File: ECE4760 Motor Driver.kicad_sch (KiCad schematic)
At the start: 45 parts, among them J1 IO, J100 Alternative Motor, J2 Motor / Power, J4 UART, J5 Debug, SW1 BOOT, U1 STM32G473V_B-C-E_Hx, U5 AP7361C-33FGE, U7 TPSM365R6, X1 48MHz

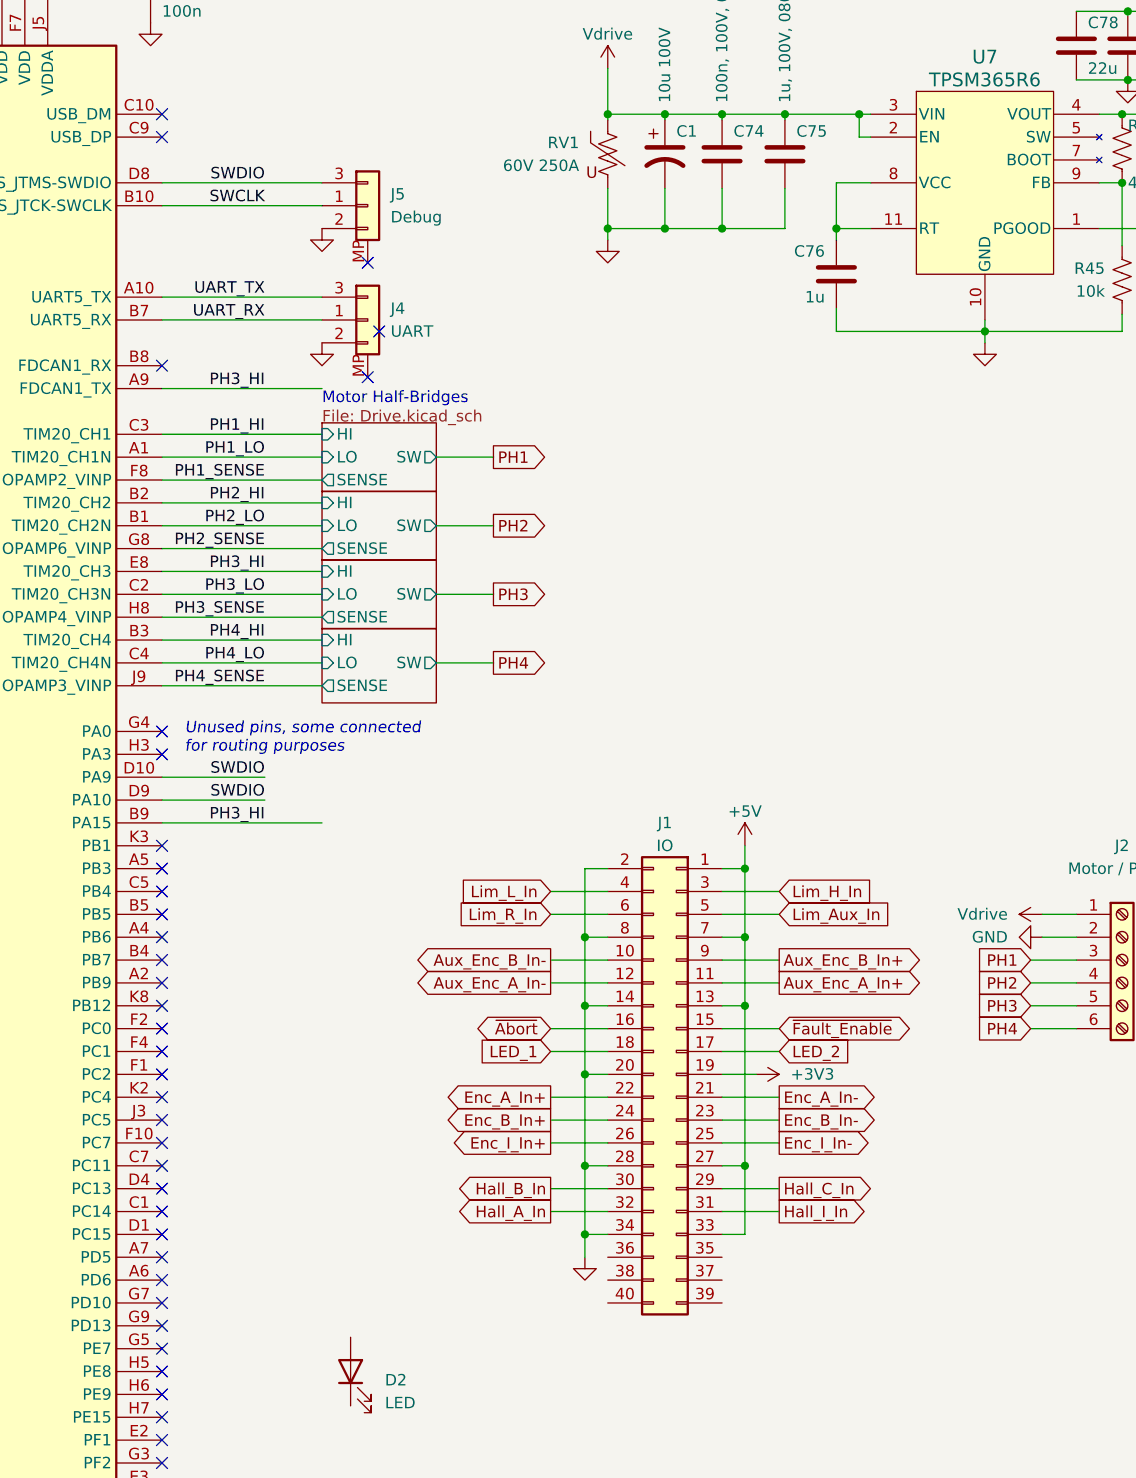
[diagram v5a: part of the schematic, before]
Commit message: Limit switch inputs and silkscreen
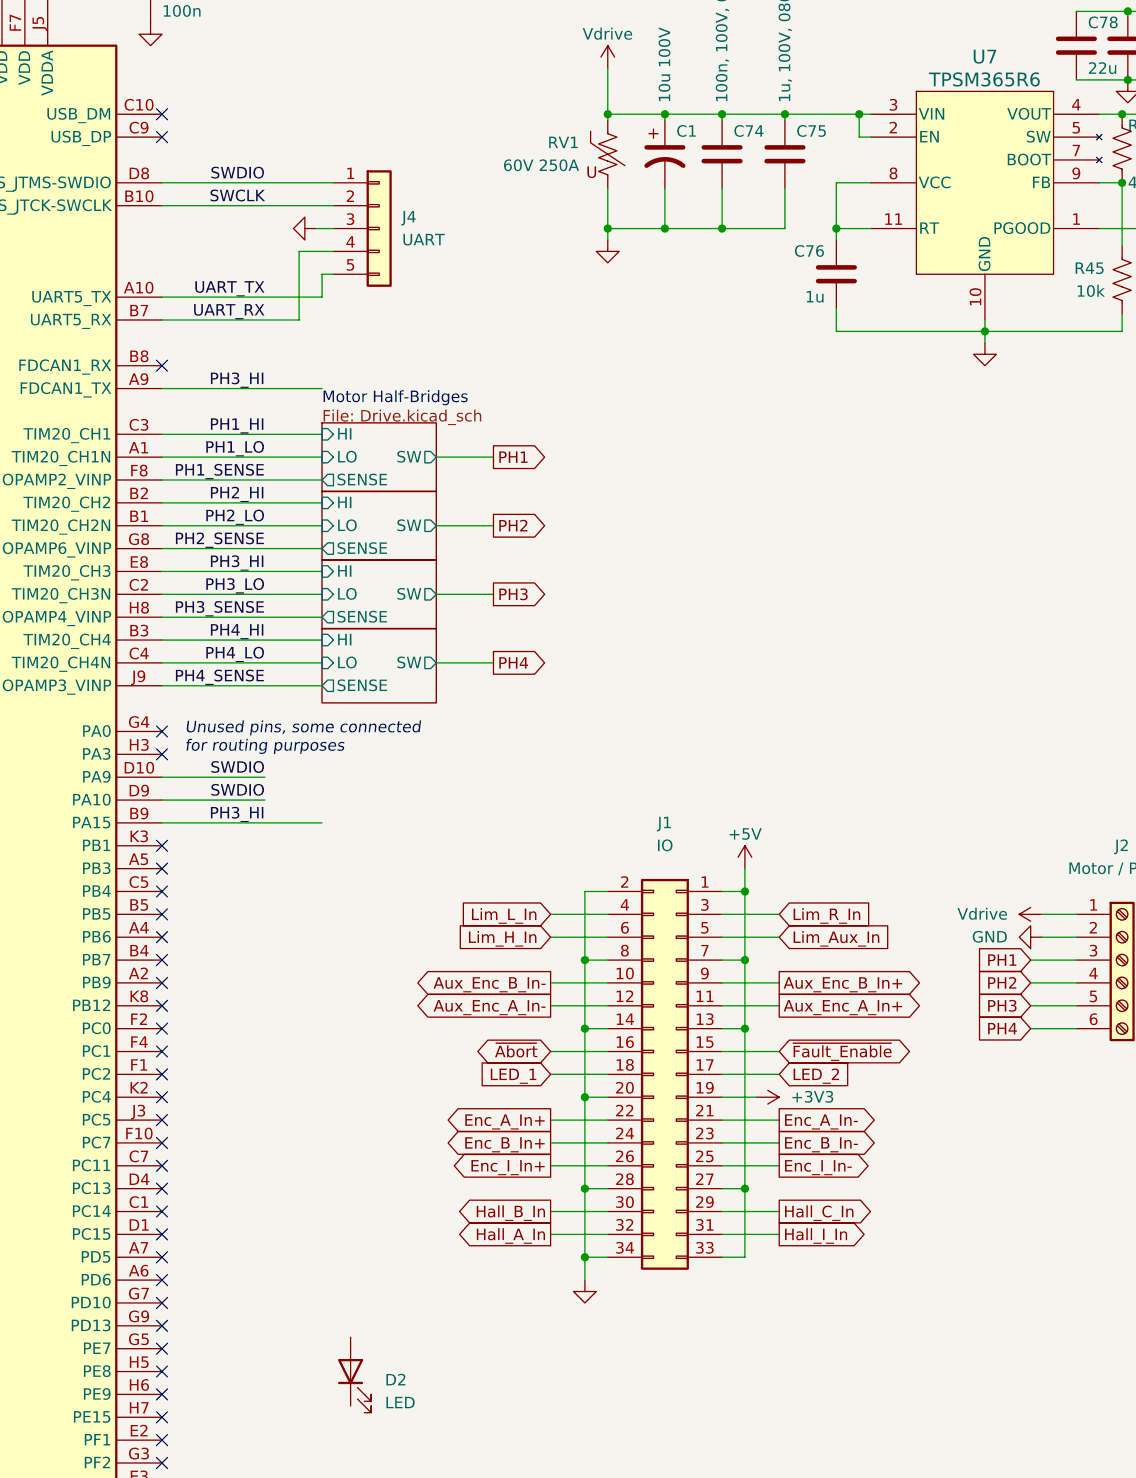
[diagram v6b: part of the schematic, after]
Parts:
- removed J5: Debug, Connector_JST:JST_GH_SM03B-GHS-TB_1x03-1MP_P1.25mm_Horizontal, symbol Connector_Generic:Conn_01x03
- C1: footprint Capacitor_THT:CP_Radial_D8.0mm_P5.00mm -> Capacitor_SMD:CP_Elec_6.3x7.7; DigiKey 1189-1513-1-ND -> (none); LCSC (none) -> C7471882
- J1: footprint Connector_PinSocket_2.54mm:PinSocket_2x20_P2.54mm_Vertical -> Connector_PinSocket_2.54mm:PinSocket_2x17_P2.54mm_Vertical; symbol Connector_Generic:Conn_02x20_Odd_Even -> Connector_Generic:Conn_02x17_Odd_Even
- J4: footprint Connector_JST:JST_GH_SM03B-GHS-TB_1x03-1MP_P1.25mm_Horizontal -> Connector_PinHeader_2.54mm:PinHeader_1x05_P2.54mm_Vertical; symbol Connector_Generic:Conn_01x03 -> Connector_Generic:Conn_01x05; DigiKey 455-SM03B-GHS-TBCT-ND -> (none); LCSC C514175 -> (none)
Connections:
- net GND: now also J4.3 (Pin_3); no longer J4.2 (Pin_2)
- net Lim_H_In: now also J1.6 (Pin_6); no longer J1.3 (Pin_3)
- net Lim_R_In: now also J1.3 (Pin_3); no longer J1.6 (Pin_6)
- net SWCLK: now also J4.2 (Pin_2)
- net SWDIO: now also J4.1 (Pin_1)
- net UART_RX: now also J4.4 (Pin_4); no longer J4.1 (Pin_1)
- net UART_TX: now also J4.5 (Pin_5); no longer J4.3 (Pin_3)
- no-connect marks 43 -> 40

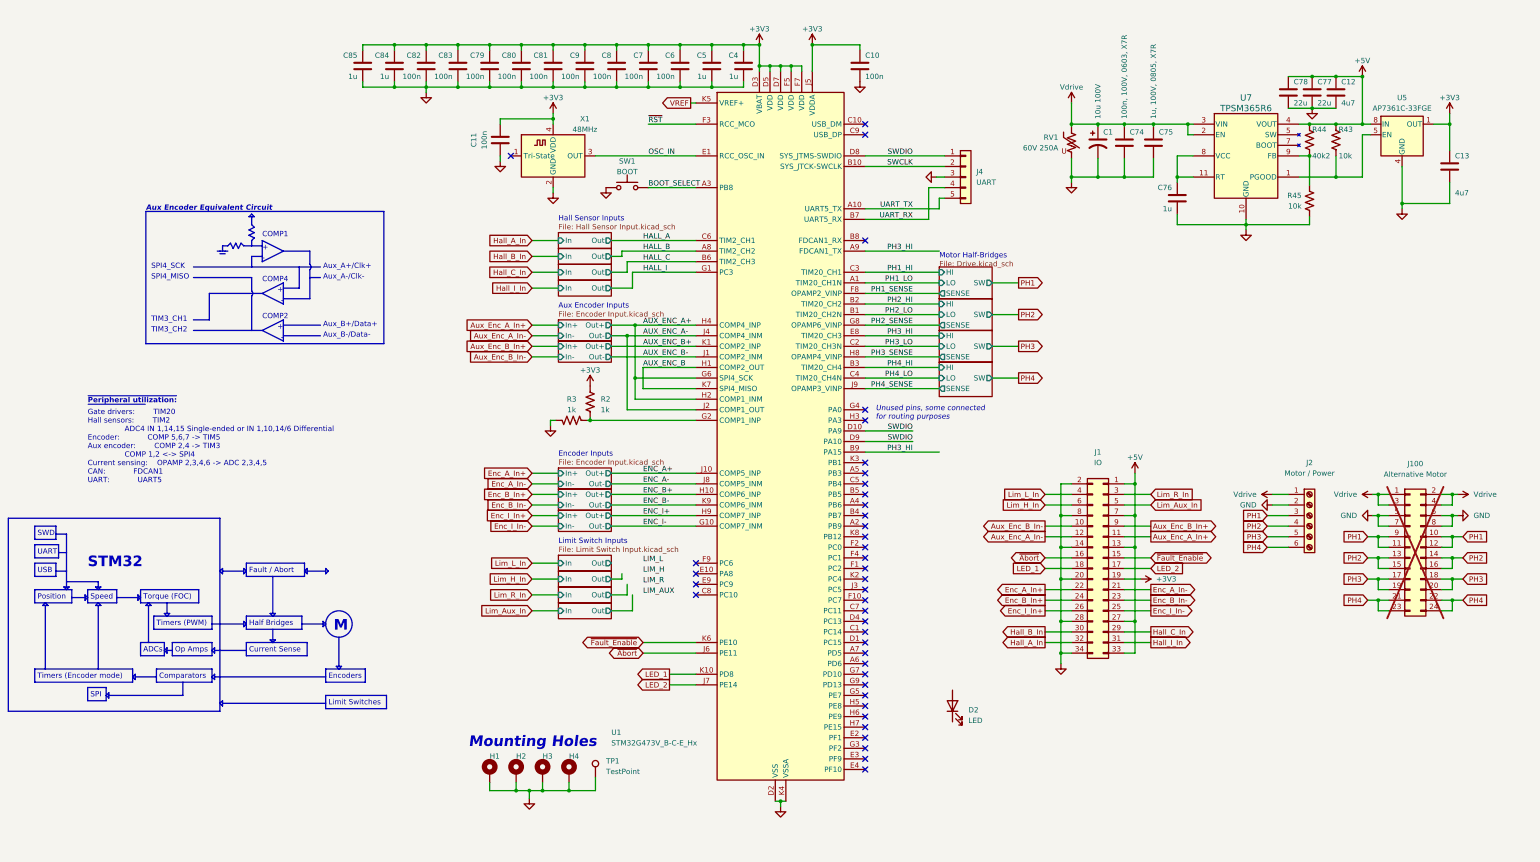
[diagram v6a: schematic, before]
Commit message: Update hall sensor circuit for 5V-tolerant pins
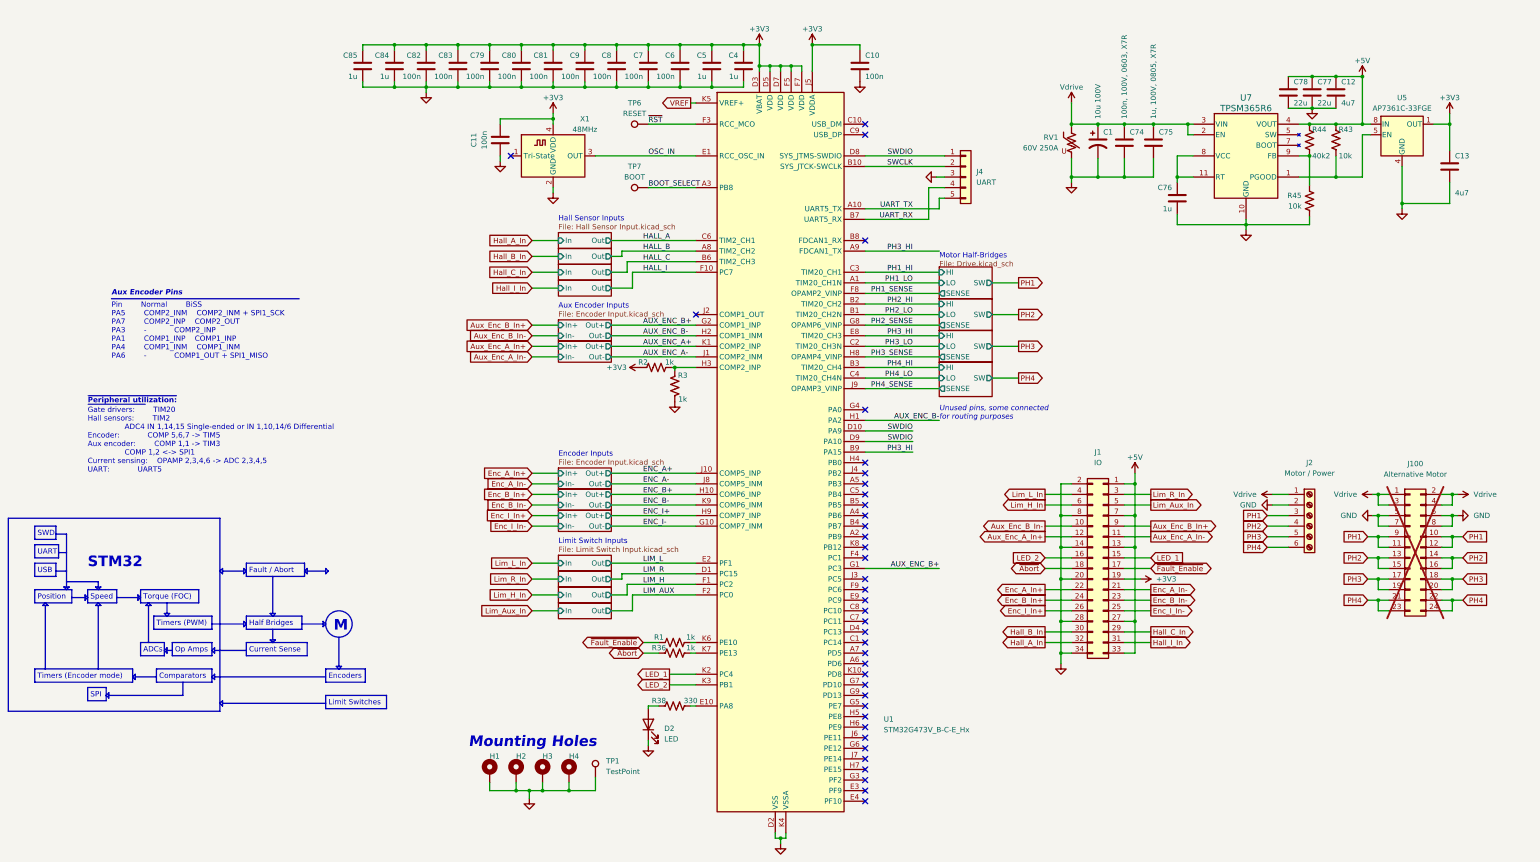
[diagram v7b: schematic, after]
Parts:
- removed SW1: BOOT, Button_Switch_SMD:SW_SPST_PTS810, symbol Switch:SW_Push
- added R1, R36: 1k, Resistor_SMD:R_0402_1005Metric, symbol Device:R_US
- added R38: 330, Resistor_SMD:R_0402_1005Metric, symbol Device:R_US
- added TP6: RESET, TestPoint:TestPoint_Pad_D2.0mm, symbol Connector:TestPoint
- added TP7: BOOT, TestPoint:TestPoint_Pad_D2.0mm, symbol Connector:TestPoint
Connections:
- net AUX_ENC_A+: now also U1.K1 (PA7); no longer U1.G6 (PE12), U1.H2 (PA4), U1.H4 (PB0)
- net AUX_ENC_A-: now also U1.J1 (PA5); no longer U1.J2 (PA6), U1.J4 (PB2)
- net AUX_ENC_B+: now also U1.G1 (PC3), U1.G2 (PA1); no longer U1.K1 (PA7)
- net AUX_ENC_B-: now also U1.H1 (PA2), U1.H2 (PA4); no longer U1.J1 (PA5)
- net Aux_Enc_A_In+: now also J1.12 (Pin_12); no longer J1.11 (Pin_11)
- net Aux_Enc_A_In-: now also J1.11 (Pin_11); no longer J1.12 (Pin_12)
- net BOOT_SELECT: now also TP7.1
- net GND: now also D2.1 (K)
- net HALL_I: now also U1.F10 (PC7); no longer U1.G1 (PC3)
- net LED_1: now also J1.15 (Pin_15), U1.K2 (PC4); no longer J1.18 (Pin_18), U1.K10 (PD8)
- net LED_2: now also J1.16 (Pin_16), U1.K3 (PB1); no longer J1.17 (Pin_17), U1.J7 (PE14)
- net LIM_AUX: now also U1.F2 (PC0)
- net LIM_H: now also U1.F1 (PC2)
- net LIM_L: now also U1.E2 (PF1)
- net LIM_R: now also U1.D1 (PC15)
- net ~{Abort}: now also J1.18 (Pin_18), R36.1; no longer J1.16 (Pin_16), U1.J6 (PE11)
- net ~{Fault_Enable}: now also J1.17 (Pin_17), R1.1; no longer J1.15 (Pin_15), U1.K6 (PE10)
- net ~{RST}: now also TP6.1
- net at R2.2, R3.1: now also U1.H3 (PA3); no longer U1.G2 (PA1)
- net at U1.E10 (PA8): now also R38.2
- net at D2.2 (A): now also R38.1
- net AUX_ENC_B: no longer names the net of U1.K7 (PE13)
- net AUX_ENC_B: now also R36.2; no longer U1.H1 (PA2)
- new net: R1.2, U1.K6 (PE10)
- no-connect marks 40 -> 38
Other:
- note added: "Aux Encoder Pins"
- note added: "Gate drivers: TIM20 Hall sensors: TIM2 ADC4 IN 1,14,15 Single-ended or IN 1,10,14/6 Differential Encoder: COMP 5,6,7 -> TIM5 Aux encoder: COMP 1,1 -> TIM3 COMP 1,2 <-> SPI1 Current sensing: OPAMP 2,3,4,6 -> ADC 2,3,4,5 UART: UART5"
- note added: "Pin Normal BiSS PA5 COMP2_INM COMP2_INM + SPI1_SCK PA7 COMP2_INP COMP2_OUT PA3 - COMP2_INP PA1 COMP1_INP COMP1_INP PA4 COMP1_INM COMP1_INM PA6 - COMP1_OUT + SPI1_MISO"
- note removed: "+"
- note removed: "-"
- note removed: "Aux Encoder Equivalent Circuit"
- note removed: "Aux_A+/Clk+"
- note removed: "Aux_A-/Clk-"
- note removed: "Aux_B+/Data+"
- note removed: "Aux_B-/Data-"
- note removed: "COMP1"
- note removed: "COMP2"
- note removed: "COMP4"
- note removed: "Gate drivers: TIM20 Hall sensors: TIM2 ADC4 IN 1,14,15 Single-ended or IN 1,10,14/6 Differential Encoder: COMP 5,6,7 -> TIM5 Aux encoder: COMP 2,4 -> TIM3 COMP 1,2 <-> SPI4 Current sensing: OPAMP 2,3,4,6 -> ADC 2,3,4,5 CAN: FDCAN1 UART: UART5"
- note removed: "SPI4_MISO"
- note removed: "SPI4_SCK"
- note removed: "TIM3_CH1"
- note removed: "TIM3_CH2"
- moved on the sheet: D2, R2, R3, U1

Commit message: Ready for design review
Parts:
- removed R1, R36: 1k, Resistor_SMD:R_0402_1005Metric, symbol Device:R_US
- removed R43: 10k, Resistor_SMD:R_0402_1005Metric, symbol Device:R_US
- added C81, C82: 100n, Capacitor_SMD:C_0402_1005Metric, symbol Device:C
- C1: value 10u 100V -> 22u 100V
- C2: renamed from C74; DigiKey 490-3285-1-ND -> 490-13420-1-ND; LCSC (none) -> C161117
- C3: renamed from C75; LCSC (none) -> C5370002
- C4: renamed from C78; DigiKey (none) -> 490-GRM21BZ71A226ME15LCT-ND; LCSC (none) -> C907991
- C5: renamed from C77; DigiKey (none) -> 490-GRM21BZ71A226ME15LCT-ND; LCSC (none) -> C907991
- C6: renamed from C12; DigiKey (none) -> 490-GRM188Z71C475KE21DCT-ND; LCSC (none) -> C389010
- C69: renamed from C10; DigiKey 490-10700-1-ND -> 490-3261-1-ND; LCSC (none) -> C71629
- C7: renamed from C76; value 1u -> 4u7; DigiKey (none) -> 490-GRM188Z71C475KE21DCT-ND; LCSC (none) -> C389010
- C70: renamed from C5; value 1u -> 4u7; DigiKey (none) -> 490-GRM188Z71C475KE21DCT-ND; LCSC (none) -> C389010
- C71: renamed from C4; value 1u -> 4u7; DigiKey (none) -> 490-GRM188Z71C475KE21DCT-ND; LCSC (none) -> C389010
- C72: renamed from C85; value 1u -> 4u7; DigiKey (none) -> 490-GRM188Z71C475KE21DCT-ND; LCSC (none) -> C389010
- C73: renamed from C84; value 1u -> 4u7; DigiKey (none) -> 490-GRM188Z71C475KE21DCT-ND; LCSC (none) -> C389010
- C74: renamed from C79; DigiKey 490-10700-1-ND -> 490-3261-1-ND; LCSC (none) -> C71629
- C75: renamed from C80; DigiKey 490-10700-1-ND -> 490-3261-1-ND; LCSC (none) -> C71629
- C76: renamed from C81; DigiKey 490-10700-1-ND -> 490-3261-1-ND; LCSC (none) -> C71629
- C77: renamed from C9; DigiKey 490-10700-1-ND -> 490-3261-1-ND; LCSC (none) -> C71629
- C78: renamed from C8; DigiKey 490-10700-1-ND -> 490-3261-1-ND; LCSC (none) -> C71629
- C79: renamed from C7; DigiKey 490-10700-1-ND -> 490-3261-1-ND; LCSC (none) -> C71629
- C8: renamed from C13; DigiKey (none) -> 490-GRM188Z71C475KE21DCT-ND; LCSC (none) -> C389010
- C80: renamed from C6; DigiKey 490-10700-1-ND -> 490-3261-1-ND; LCSC (none) -> C71629
- C83: renamed from C82; DigiKey 490-10700-1-ND -> 490-3261-1-ND; LCSC (none) -> C71629; now not fitted; now left out of the parts list
- C84: renamed from C83; DigiKey 490-10700-1-ND -> 490-3261-1-ND; LCSC (none) -> C71629; now not fitted; now left out of the parts list
- C85: renamed from C11; DigiKey 490-10700-1-ND -> 490-3261-1-ND; LCSC (none) -> C71629
- D5: renamed from D2; value LED -> Green; DigiKey (none) -> 160-2018-1-ND; LCSC (none) -> C364563
- R1: renamed from R44; DigiKey 311-1.00KLRCT-ND -> 311-40.2KLRCT-ND; LCSC (none) -> C137983
- R28: renamed from R2; LCSC (none) -> C2935237
- R29: renamed from R3; LCSC (none) -> C2935237
- R3: renamed from R45; DigiKey 311-1.00KLRCT-ND -> 311-10.0KLRCT-ND; LCSC (none) -> C60490
- R30: renamed from R38; DigiKey (none) -> 311-330KLRCT-ND; LCSC (none) -> C138006
- TP1: renamed from TP6; now left out of the parts list
- TP2: renamed from TP7; now left out of the parts list
- TP?: renamed from TP1; value TestPoint -> Sense
- renumbered J100 to J101, J4 to J3, U5 to U6
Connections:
- net VREF is gone; now on net +3V3: U1.K5 (VREF+)
- net +3V3: now also C81.1, C82.1
- net +5V: now also U6.5 (EN)
- net AUX_ENC_A-: now also U1.G6 (PE12)
- net ENC_I+: now also U1.F10 (PC7), U1.G9 (PD13)
- net GND: now also C81.2, C82.2
- net HALL_I: now also U1.F9 (PC6); no longer U1.F10 (PC7)
- net PH4_LO: now also U1.B4 (PB7)
- net ~{Abort}: now also U1.J6 (PE11)
- net ~{Fault_Enable}: now also U1.K6 (PE10)
- net at U7.1 (PGOOD): no longer U6.5 (EN)
- net at U1.K7 (PE13): now also U1.J2 (PA6)
- no-connect marks 38 -> 33
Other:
- note added: "Decoupling capacitors, place close to U1 on all sides"
- moved on the sheet: C1, C2, C3, C4, C5, C6, C69, C7, C70, C71, C72, C73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
